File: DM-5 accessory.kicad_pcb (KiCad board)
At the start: 2 copper layers, 18 parts, among them J1 24VAC, J2 Input, J3 Output, U1 LR645N3

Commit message: respin
better foorprints, single sided board
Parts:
- C1: value 1.0 uF -> 10.0 uF 63V; footprint Capacitors_THT:C_Axial_L5.1mm_D3.1mm_P7.50mm_Horizontal -> Capacitors_THT:CP_Radial_D10.0mm_P2.50mm_P5.00mm
- C2: value .1 uF -> 1.0 uF 63V; footprint Capacitors_THT:C_Disc_D3.8mm_W2.6mm_P2.50mm -> Capacitors_THT:CP_Radial_D10.0mm_P2.50mm_P5.00mm
- D1, D2, D3, D4: footprint Diodes_THT:D_A-405_P7.62mm_Horizontal -> Diodes_THT:D_DO-35_SOD27_P10.16mm_Horizontal
- F1: value 1A 250V -> 1A ATC; footprint Fuse_Holders_and_Fuses:Fuseholder_ATO_Blade_littlefuse_Pudenz_2_Pin -> Fuse_Holders_and_Fuses:BladeFuse-CarType
- F2: value Polyfuse 0.08A -> Polyfuse 6mA; footprint Varistors:RV_Disc_D7_W3.4_P5 -> Varistors:RV_Disc_D7_W4.8_P5
- J1, J3: footprint Connectors_Terminal_Blocks:TerminalBlock_4UCON_19963_02x3.5mm_Straight -> Connectors_Terminal_Blocks:TerminalBlock_Pheonix_PT-3.5mm_2pol
- J2: footprint Connectors_Terminal_Blocks:TerminalBlock_4UCON_19963_04x3.5mm_Straight -> Connectors_Terminal_Blocks:TerminalBlock_Pheonix_PT-3.5mm_4pol
- R1, R2, R3, R4, R5, R6: footprint Resistors_THT:R_Axial_DIN0204_L3.6mm_D1.6mm_P5.08mm_Horizontal -> Resistors_THT:R_Axial_DIN0207_L6.3mm_D2.5mm_P7.62mm_Horizontal
- U1: footprint TO_SOT_Packages_THT:TO-92_Inline_Narrow_Oval -> TO_SOT_Packages_THT:TO-220-3_Vertical
- moved J3 74.3 mm to (219.7, 124.5)
- moved R5 52.5 mm to (223.5, 114.3)
- moved R6 50.9 mm to (223.5, 101.6)
- moved J2 48.5 mm to (210.8, 92.7)
- moved R4 48.4 mm to (215.9, 101.6)
- moved R3 45.7 mm to (212.1, 114.3), turned to 180 degrees
- moved R1 42.1 mm to (204.5, 101.6)
- moved F2 39.5 mm to (196.8, 102.9)
- moved R2 35.6 mm to (198.1, 114.3)
- moved D4 30.0 mm to (144.8, 105.4)
- moved F1 20.9 mm to (141.0, 96.5), turned to 180 degrees
- moved D2 20.7 mm to (128.3, 114.3)
- moved U1 19.2 mm to (174.0, 121.9), turned to 90 degrees
- moved C2 18.5 mm to (186.7, 119.4), turned to 270 degrees
- moved J1 18.0 mm to (153.7, 96.5)
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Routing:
- net Net-(D3-Pad2): track 54.5 -> 24.1 mm
- net Net-(J3-Pad1): track 46.6 -> 16.8 mm
- net Net-(C1-Pad2): track 67.6 -> 94.9 mm
- net Net-(C1-Pad1): track 15.2 -> 36.6 mm
- net Net-(D1-Pad2): track 12.1 -> 27.3 mm
- net Net-(C2-Pad1): track 35.5 -> 44.7 mm
- net Net-(F2-Pad1): track 9.72 -> 18.2 mm
- net Net-(J2-Pad2): track 9.07 -> 14.5 mm
- net Net-(F1-Pad1): track 17.8 -> 12.7 mm
- net Net-(J2-Pad4): track 7.76 -> 9.80 mm
- net Net-(R3-Pad1): track 10.7 -> 8.89 mm
- net Net-(J2-Pad3): track 8.42 -> 9.69 mm

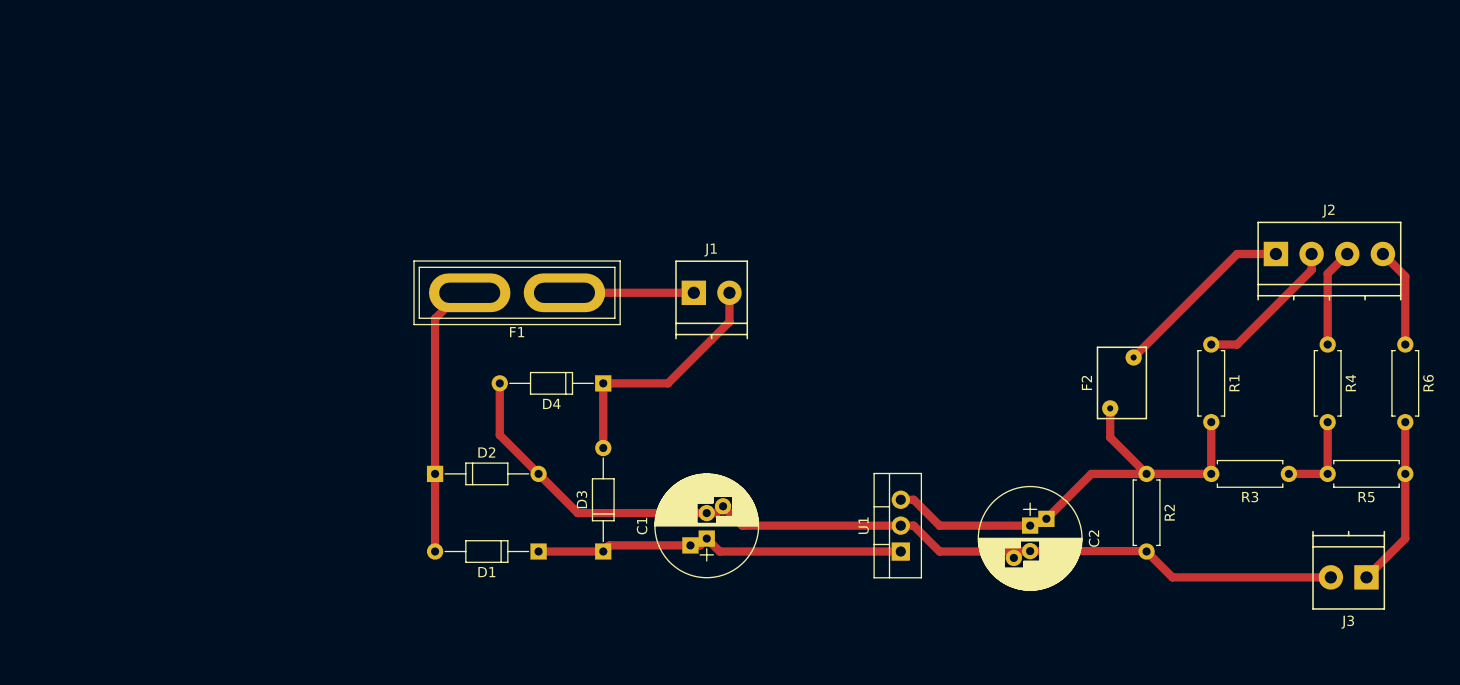
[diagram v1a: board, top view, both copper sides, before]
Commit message: respin
swap LR645 -> LR8
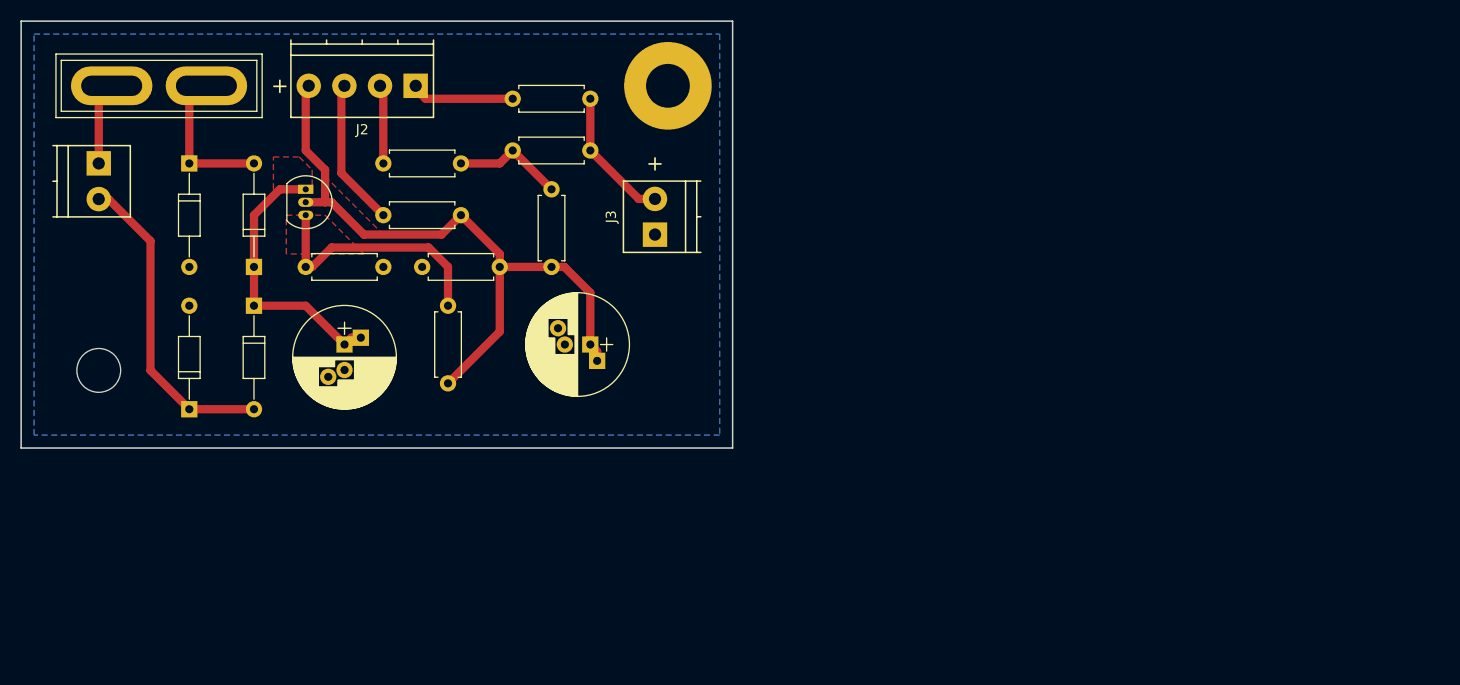
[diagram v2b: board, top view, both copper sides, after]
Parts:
- removed D1, D2: D, Diodes_THT:D_DO-35_SOD27_P10.16mm_Horizontal
- removed F2: Polyfuse 6mA, Varistors:RV_Disc_D7_W4.8_P5
- added 1N4148: D, Diodes_THT:D_DO-35_SOD27_P10.16mm_Horizontal, F.Cu at (110.5, 94.0)
- added D: 1N4148, Diodes_THT:D_DO-35_SOD27_P10.16mm_Horizontal, F.Cu at (104.1, 83.8)
- added R7: 1K2, Resistors_THT:R_Axial_DIN0207_L6.3mm_D2.5mm_P7.62mm_Horizontal, F.Cu at (123.2, 94.0)
- added R8: 8K8, Resistors_THT:R_Axial_DIN0207_L6.3mm_D2.5mm_P7.62mm_Horizontal, F.Cu at (129.5, 97.8)
- added REF**: MountingHole_4.3mm_M4_Pad, Mounting_Holes:MountingHole_4.3mm_M4_Pad, B.Cu at (151.1, 76.2)
- added REF**: MountingHole_4.3mm_M4, Mounting_Holes:MountingHole_4.3mm_M4, F.Cu at (95.2, 104.1)
- U1: value LR645N3 -> LR8; footprint TO_SOT_Packages_THT:TO-220-3_Vertical -> TO_SOT_Packages_THT:TO-92_Inline_Narrow_Oval
- moved R4 94.4 mm to (123.2, 83.8), turned to 0 degrees
- moved R6 90.9 mm to (135.9, 77.5), turned to 0 degrees
- moved R5 86.1 mm to (143.5, 82.5)
- moved J2 86.1 mm to (126.4, 76.2), turned to 180 degrees
- moved R1 82.3 mm to (123.2, 88.9), turned to 0 degrees
- moved R3 77.6 mm to (139.7, 86.4), turned to 270 degrees
- moved J3 77.5 mm to (149.9, 90.8), turned to 90 degrees
- moved U1 68.4 mm to (115.6, 86.4), turned to 270 degrees
- moved R2 66.7 mm to (134.6, 94.0), turned to 180 degrees
- moved J1 59.8 mm to (95.2, 83.8), turned to 270 degrees
- moved F1 48.9 mm to (96.5, 76.2), turned to 0 degrees
- moved C2 46.7 mm to (143.5, 101.6), turned to 180 degrees
- moved D3 41.9 mm to (110.5, 97.8), turned to 270 degrees
- moved D4 40.7 mm to (104.1, 108.0), turned to 90 degrees
- moved C1 40.3 mm to (119.4, 101.6), turned to 270 degrees
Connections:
- J2 pad 1: Net-(F2-Pad1) -> Net-(J2-Pad1)
- J2 pad 4: Net-(J2-Pad4) -> Net-(C2-Pad1)
- J3 pad 1: Net-(J3-Pad1) -> Net-(C1-Pad2)
- J3 pad 2: Net-(C1-Pad2) -> Net-(J3-Pad2)
- R1 pad 1: Net-(J2-Pad2) -> Net-(J2-Pad3)
- R4 pad 1: Net-(J2-Pad3) -> Net-(J2-Pad2)
- R5 pad 1: Net-(J3-Pad1) -> Net-(J3-Pad2)
- R6 pad 1: Net-(J2-Pad4) -> Net-(J2-Pad1)
- R6 pad 2: Net-(J3-Pad1) -> Net-(J3-Pad2)
- U1 pad 2: Net-(C1-Pad2) -> Net-(C2-Pad1)
- U1 pad 3: Net-(C2-Pad1) -> Net-(R7-Pad2)
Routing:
- net Net-(C1-Pad2): track 94.9 -> 0.00 mm
- net Net-(R7-Pad2): track 0.00 -> 24.4 mm
- net Net-(C2-Pad1): track 44.7 -> 66.7 mm
- net Net-(F2-Pad1): track 18.2 -> 0.00 mm
- net Net-(J3-Pad1): track 16.8 -> 0.00 mm
- net Net-(J3-Pad2): track 0.00 -> 13.4 mm
- net Net-(D1-Pad2): track 27.3 -> 14.7 mm
- net Net-(J2-Pad1): track 0.00 -> 10.3 mm
- net Net-(J2-Pad4): track 9.80 -> 0.00 mm
- net Net-(C1-Pad1): track 36.6 -> 27.4 mm
- net Net-(D3-Pad2): track 24.1 -> 31.2 mm
- net Net-(J2-Pad2): track 14.5 -> 7.88 mm
- net Net-(J2-Pad3): track 9.69 -> 14.4 mm
- net Net-(F1-Pad1): track 12.7 -> 8.15 mm
- net Net-(R3-Pad1): track 8.89 -> 11.0 mm
- added copper zone on F.Cu, net Net-(C1-Pad1)
- added copper zone on B.Cu, net Net-(C1-Pad2)
- added copper zone on F.Cu, net Net-(C2-Pad1)
- added copper zone on F.Cu, net Net-(R7-Pad2)
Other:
- board outline added: 69.8 x 41.9 mm
- board text added: "+"
